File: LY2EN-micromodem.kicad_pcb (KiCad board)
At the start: 2 copper layers, 19 parts, among them Q1 2N7000

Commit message: PCB version 0.1
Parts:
- added _: SolderWire, Connector_Wire:SolderWire-0.5sqmm_1x04_P4.6mm_D0.9mm_OD2.1mm, F.Cu at (87.6, 33.0)
- C1, C2, C3: footprint Capacitor_SMD:C_1812_4532Metric_Pad1.57x3.40mm_HandSolder -> Capacitor_SMD:C_0805_2012Metric_Pad1.18x1.45mm_HandSolder
- R1, R10, R11, R16, R2, R3, R4, R6, R7, R8, R9: footprint Resistor_SMD:R_1812_4532Metric_Pad1.30x3.40mm_HandSolder -> Resistor_SMD:R_0805_2012Metric_Pad1.20x1.40mm_HandSolder
- R5: footprint Potentiometer_SMD:Potentiometer_Vishay_TS53YL_Vertical -> Potentiometer_THT:Potentiometer_Bourns_3296W_Vertical
- RX1, TX1: footprint LED_SMD:LED_1812_4532Metric_Pad1.30x3.40mm_HandSolder -> LED_SMD:LED_0805_2012Metric_Pad1.15x1.40mm_HandSolder
- moved C3 32.1 mm to (98.3, 69.6)
- moved R16 31.2 mm to (91.9, 87.9)
- moved R11 28.8 mm to (98.3, 80.2)
- moved Q1 28.2 mm to (89.2, 40.4), turned to 90 degrees
- moved R8 27.5 mm to (95.8, 87.9)
- moved R10 26.7 mm to (98.3, 75.7), turned to 270 degrees
- moved R7 24.0 mm to (92.3, 58.0)
- moved TX1 23.8 mm to (100.3, 91.9), turned to 180 degrees
- moved R9 22.2 mm to (89.7, 48.5), turned to 0 degrees
- moved RX1 19.8 mm to (87.4, 91.9), turned to 180 degrees
- moved R6 19.6 mm to (96.0, 47.7)
- moved R1 18.5 mm to (90.0, 71.1), turned to 0 degrees
- moved C2 17.1 mm to (93.5, 47.8)
- moved R2 16.1 mm to (90.0, 68.6), turned to 0 degrees
- moved C1 15.7 mm to (92.3, 60.6), turned to 0 degrees
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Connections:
- A1 pad 29: Net-(A1-Pad29) -> GND
- A1 pad 4: Net-(A1-Pad29) -> GND
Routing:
- net GND: track 0.00 -> 97.6 mm, vias 0 -> 5
- net ANALOG_IN: track 0.00 -> 38.0 mm
- net Net-(A1-Pad6): track 0.00 -> 26.3 mm
- net Net-(C1-Pad1): track 0.00 -> 23.3 mm
- net Net-(A1-Pad12): track 0.00 -> 23.0 mm
- net ANALOG_OUT: track 0.00 -> 17.0 mm
- net Net-(A1-Pad13): track 0.00 -> 14.2 mm
- net Net-(A1-Pad19): track 0.00 -> 13.0 mm
- net Net-(C2-Pad1): track 0.00 -> 10.6 mm
- net Net-(R8-Pad1): track 0.00 -> 6.85 mm
- net PTT_V+: track 0.00 -> 6.10 mm
- net Net-(A1-Pad17): track 0.00 -> 5.86 mm
- net Net-(R16-Pad1): track 0.00 -> 4.82 mm
- net Net-(A1-Pad10): track 0.00 -> 2.93 mm
- net Net-(A1-Pad8): track 0.00 -> 2.66 mm
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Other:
- board text added: "GND"
- board text added: "IN"
- board text added: "OUT"
- board text added: "PTT"

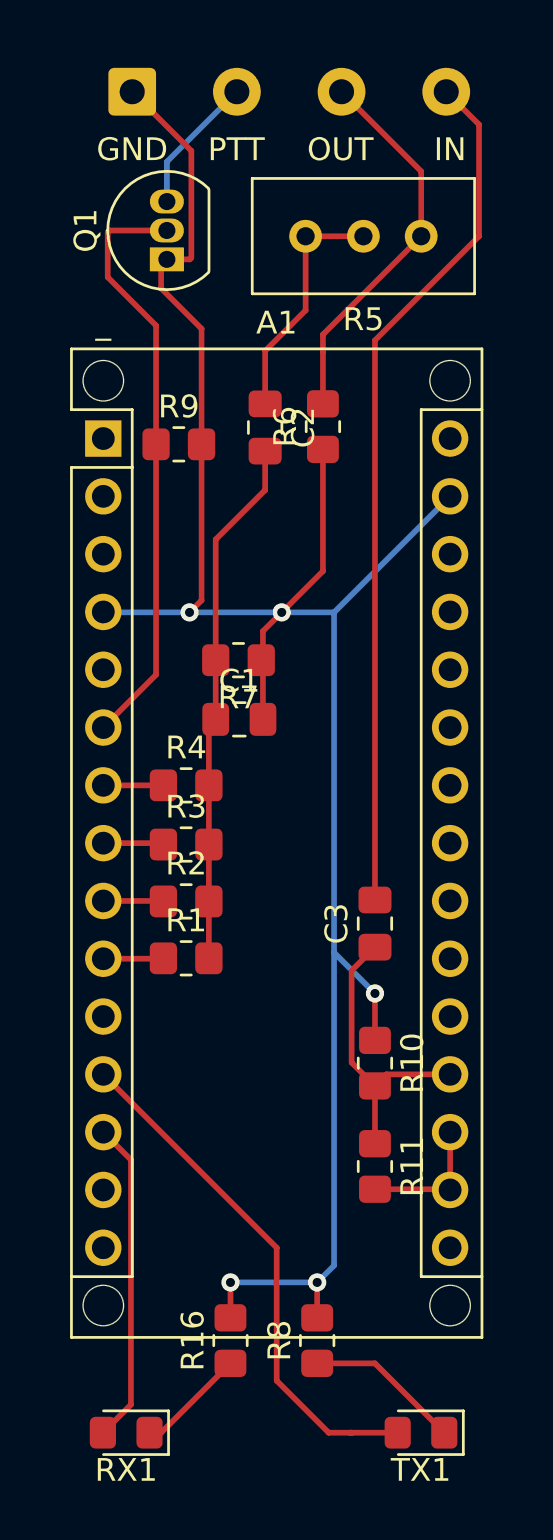
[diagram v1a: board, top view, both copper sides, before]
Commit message: Improved PCB layout: 0.5mm tracks and GND zone
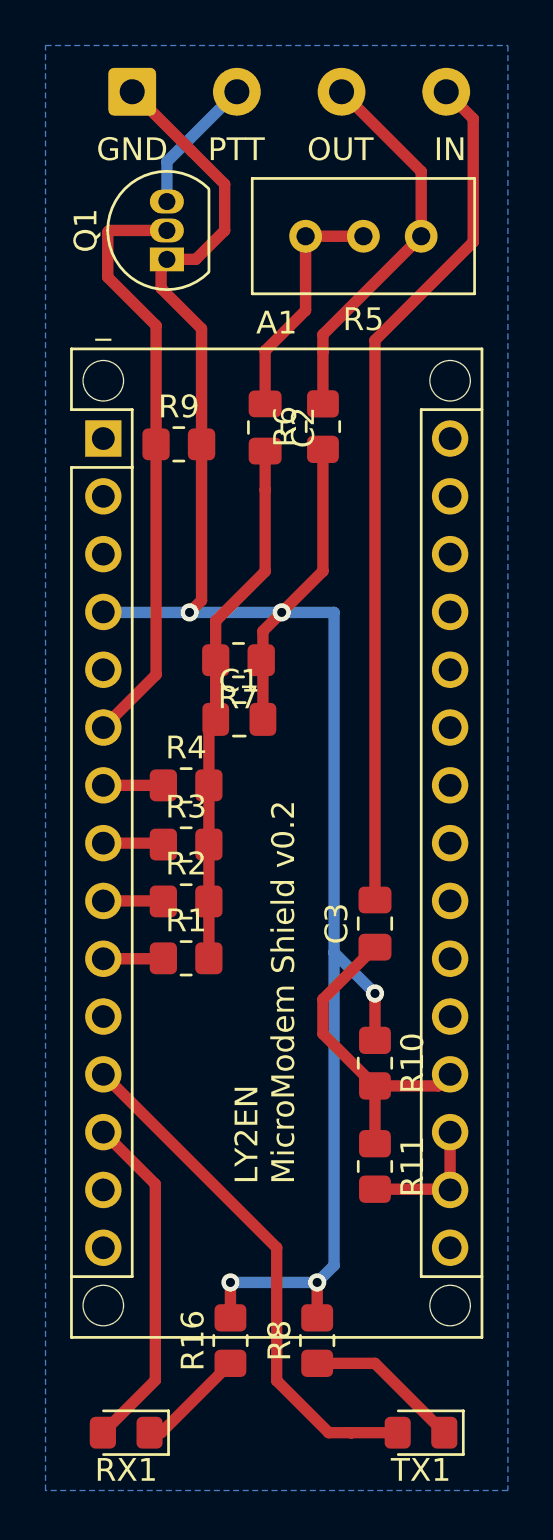
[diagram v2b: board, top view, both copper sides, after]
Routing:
- net GND: track 97.6 -> 91.8 mm
- net Net-(A1-Pad19): track 13.0 -> 14.0 mm
- net Net-(A1-Pad13): track 14.2 -> 15.1 mm
- added copper zone on B.Cu, net GND
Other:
- board text added: "LY2EN MicroModem Shield v0.2"

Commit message: Upgrade to KiCad version 6
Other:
- net class Default removed

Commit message: Bump to version 0.3
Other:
- board outline added: 20.4 x 63.5 mm
- board text added: "LY2EN MicroModem Shield v0.3"
- board text removed: "LY2EN MicroModem Shield v0.2"

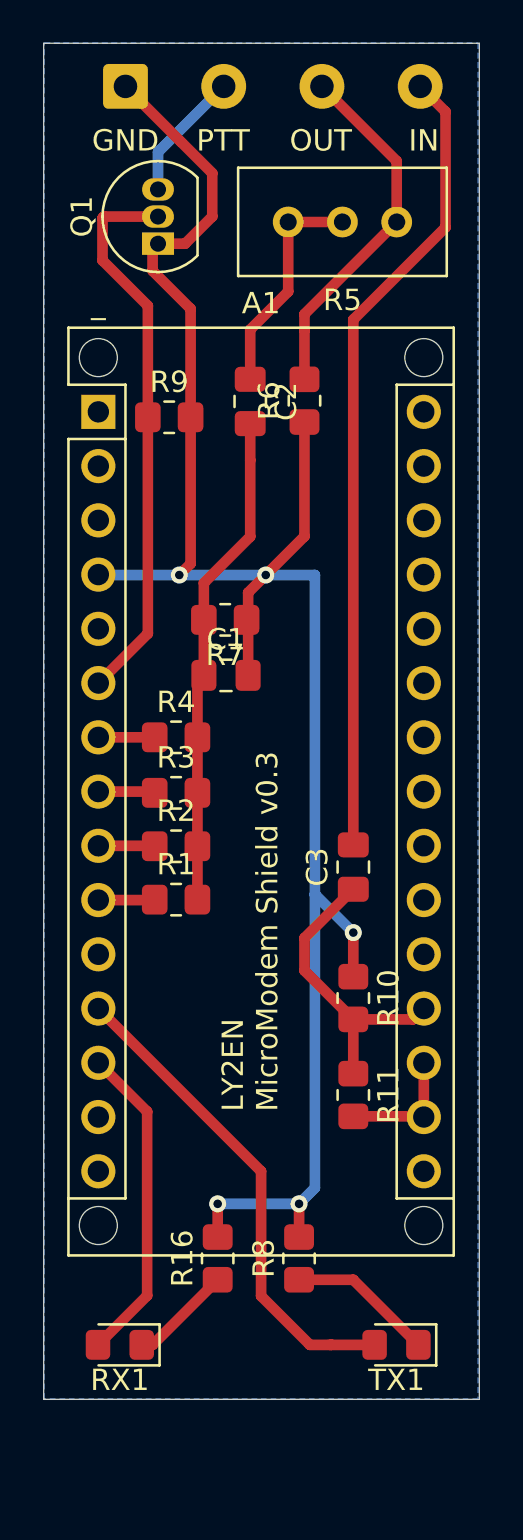
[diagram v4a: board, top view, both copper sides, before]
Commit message: Add Bluetooth SPP-C serial passthrough support
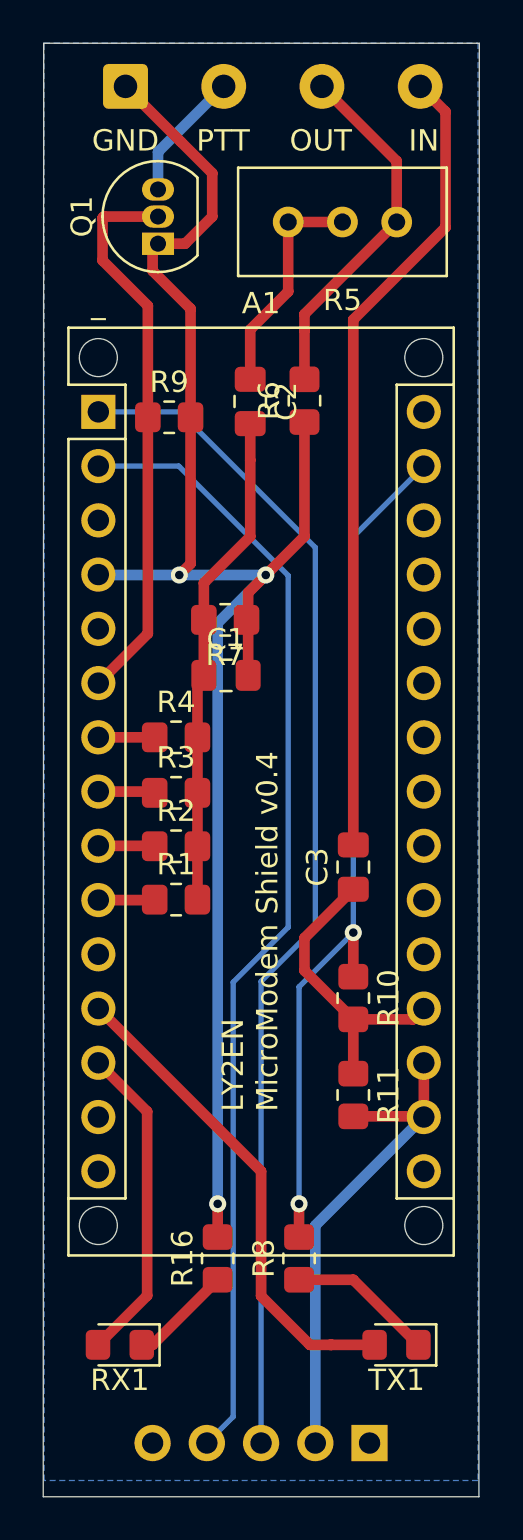
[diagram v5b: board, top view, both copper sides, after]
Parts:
- added Conn_01x05: BT_MOD, Connector_PinSocket_2.54mm:PinSocket_1x05_P2.54mm_Vertical, B.Cu at (99.1, 96.5)
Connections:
- A1 pad 11: Net-(A1-Pad11) -> unconnected-(A1-Pad11)
- A1 pad 14: Net-(A1-Pad14) -> unconnected-(A1-Pad14)
- A1 pad 15: Net-(A1-Pad15) -> unconnected-(A1-Pad15)
- A1 pad 16: Net-(A1-Pad16) -> unconnected-(A1-Pad16)
- A1 pad 20: Net-(A1-Pad20) -> unconnected-(A1-Pad20)
- A1 pad 21: Net-(A1-Pad21) -> unconnected-(A1-Pad21)
- A1 pad 22: Net-(A1-Pad22) -> unconnected-(A1-Pad22)
- A1 pad 23: Net-(A1-Pad23) -> unconnected-(A1-Pad23)
- A1 pad 24: Net-(A1-Pad24) -> unconnected-(A1-Pad24)
- A1 pad 25: Net-(A1-Pad25) -> unconnected-(A1-Pad25)
- A1 pad 26: Net-(A1-Pad26) -> unconnected-(A1-Pad26)
- A1 pad 27: Net-(A1-Pad27) -> unconnected-(A1-Pad27)
- A1 pad 28: Net-(A1-Pad28) -> unconnected-(A1-Pad28)
- A1 pad 3: Net-(A1-Pad3) -> unconnected-(A1-Pad3)
- A1 pad 30: Net-(A1-Pad30) -> unconnected-(A1-Pad30)
- A1 pad 5: Net-(A1-Pad5) -> unconnected-(A1-Pad5)
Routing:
- net Net-(Conn_01x05-Pad3): track 0.00 -> 55.8 mm
- net Net-(Conn_01x05-Pad4): track 0.00 -> 53.2 mm
- net GND: track 91.8 -> 120.7 mm
- net Net-(A1-Pad17): track 5.86 -> 23.2 mm
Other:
- board size 20.4 x 63.5 mm -> 20.4 x 68.1 mm
- board text added: "LY2EN MicroModem Shield v0.4"
- board text removed: "LY2EN MicroModem Shield v0.3"
